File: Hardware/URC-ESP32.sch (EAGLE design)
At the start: 94 parts, among them IC1 MCP9808-MSOP8, IC2 ESPWROOM32, IC3 LM358D, IC4 W5500-LQFP, IC5 CP2102N-A01-GQFN24, J1 SPI-LCD, J10 microSD, J2 I2CBR, J3 USB-C-16P-16P, J4 DC IN, J6 PWR_LED, Q1 FDN340P, Q2 MMDT3904, U1 HY931147C-RJ45

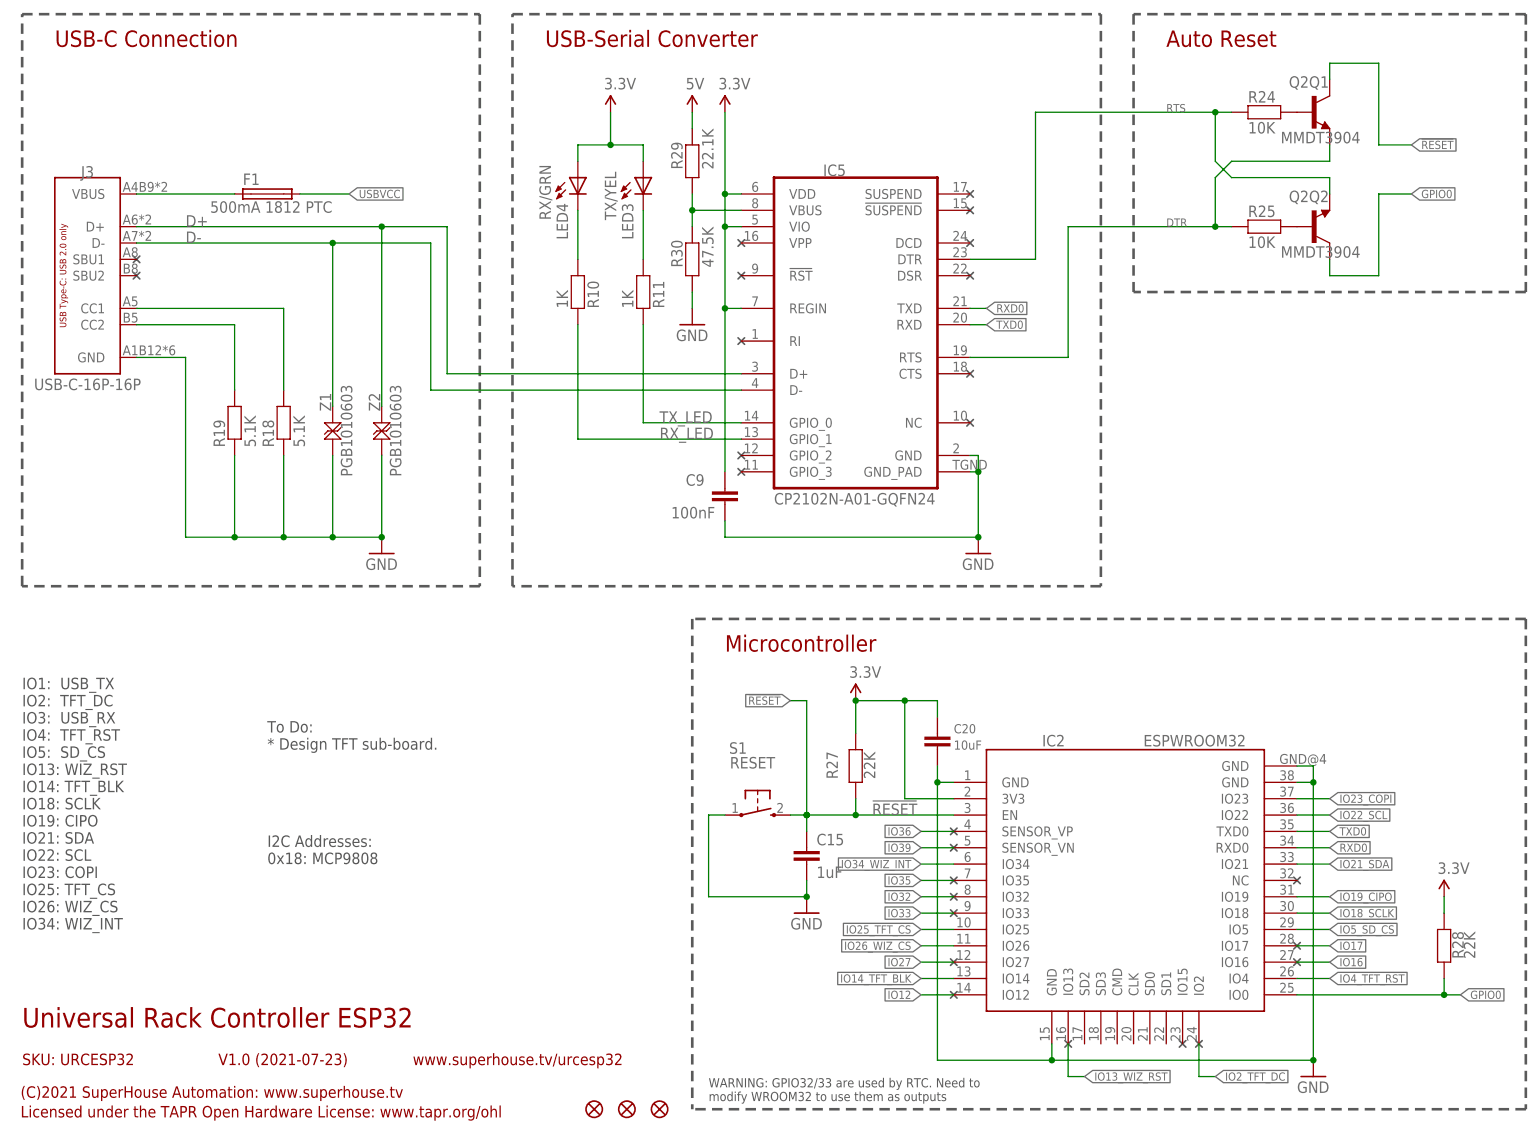
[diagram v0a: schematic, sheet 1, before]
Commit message: Added I/O header with spare pins for I2C port 2 and serial port 2.
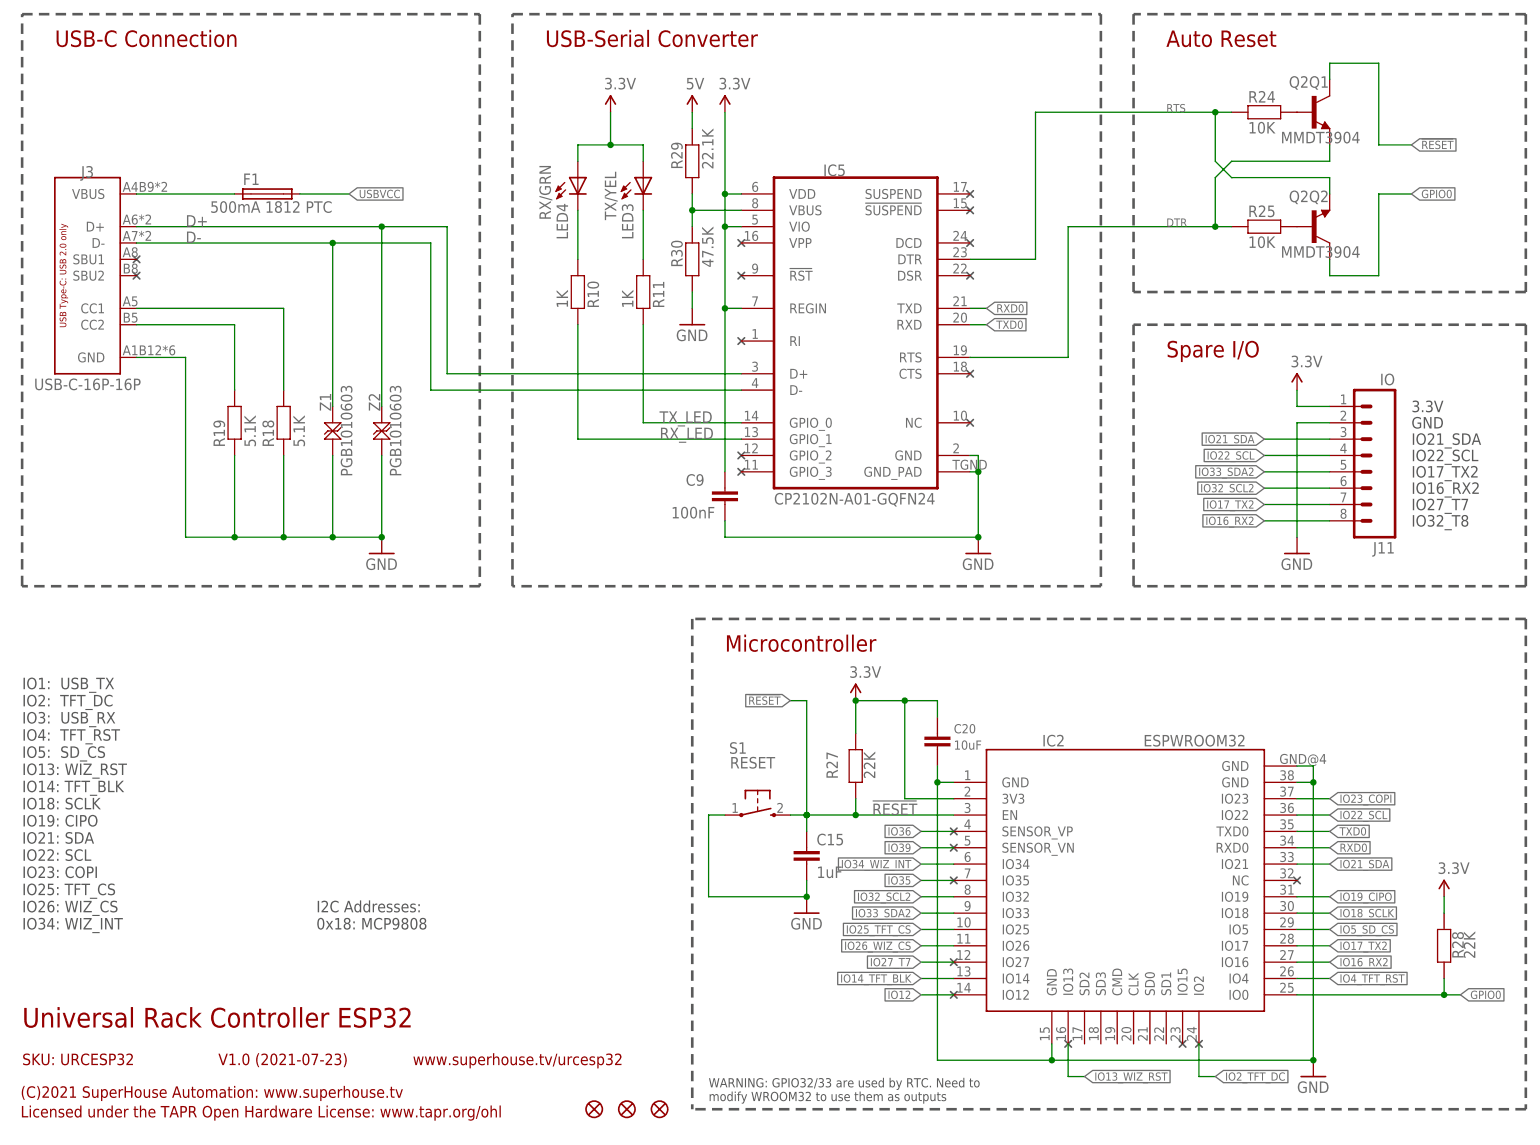
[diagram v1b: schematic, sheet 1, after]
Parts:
- added J11: IO, SuperHouse-Connectors:M08-PLAIN
- C1, C10, C11, C12, C13, C14, C15, C16, C2, C3, C4, C5, C6, C7, C8, C9: device SuperHouse-DiscreteSemi:CAP0603 -> SuperHouse-Capacitors:CAP0603
- C17: device SuperHouse-DiscreteSemi:CAP_POL1206 -> SuperHouse-Capacitors:CAP_POL1206
- C20: device SuperHouse-DiscreteSemi:CAP0805 -> SuperHouse-Capacitors:CAP0805
- D1, D2: device SuperHouse-DiscreteSemi:DIODESMA -> SuperHouse-Diodes:DIODESMA
- Q1: device freetronics-master-v1:MOSFET-PCHANNEL -> SuperHouse-Transistors:MOSFET-PCHANNEL-SMT
- Q2: device SuperHouse-DiscreteSemi:TRANS_NPN_DUAL-MMDT3904 -> SuperHouse-Transistors:TRANS_NPN_DUAL-MMDT3904
- R1, R10, R11, R14, R15, R16, R17, R18, R19, R22, R23, R24, R25, R26, R27, R28, R29, R30, R31: device SuperHouse-DiscreteSemi:RESISTOR0603 -> SuperHouse-Resistors:RESISTOR0603
- RN1, RN2: device SuperHouse-DiscreteSemi:4R-NCAY16 -> SuperHouse-Resistors:4R-NCAY16
- Z1, Z2: device SuperHouse-DiscreteSemi:TVS0603 -> SuperHouse-Diodes:TVS0603
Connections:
- net IO27 renamed IO27_T7
- removed net IO16: IC2.IO16
- removed net IO17: IC2.IO17
- removed net IO32: IC2.IO32
- removed net IO33: IC2.IO33
- new net IO16_RX2: IC2.IO16, J11.8
- new net IO17_TX2: IC2.IO17, J11.7
- new net IO32_SCL2: IC2.IO32, J11.6
- new net IO33_SDA2: IC2.IO33, J11.5
- net 3.3V: now also J11.1
- net GND: now also J11.2
- net IO21_SDA: now also J11.3
- net IO22_SCL: now also J11.4
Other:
- note added: "3.3V"
- note added: "GND"
- note added: "IO16_RX2"
- note added: "IO17_TX2"
- note added: "IO21_SDA"
- note added: "IO22_SCL"
- note added: "IO27_T7"
- note added: "IO32_T8"
- note added: "Spare I/O"
- note removed: "To Do: * Design TFT sub-board."

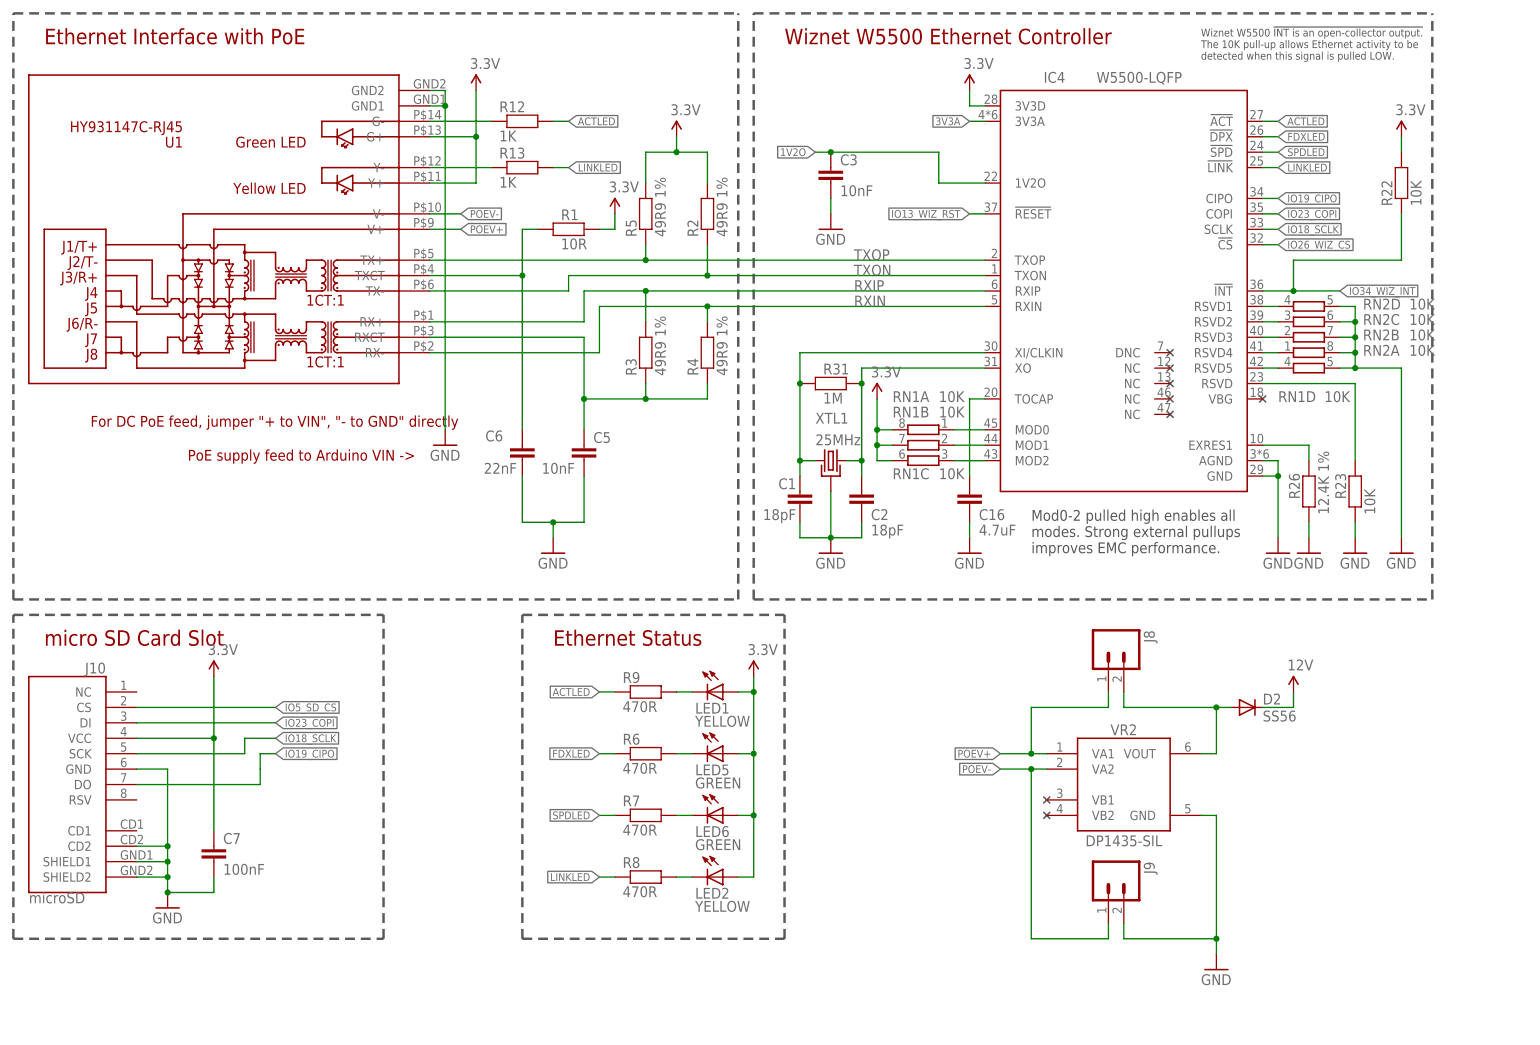
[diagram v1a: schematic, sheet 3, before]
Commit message: Fixed pin allocation notes and labels in schematic. Renamed mechanical PDF to clarify its purpose. Generated schematic PDF.
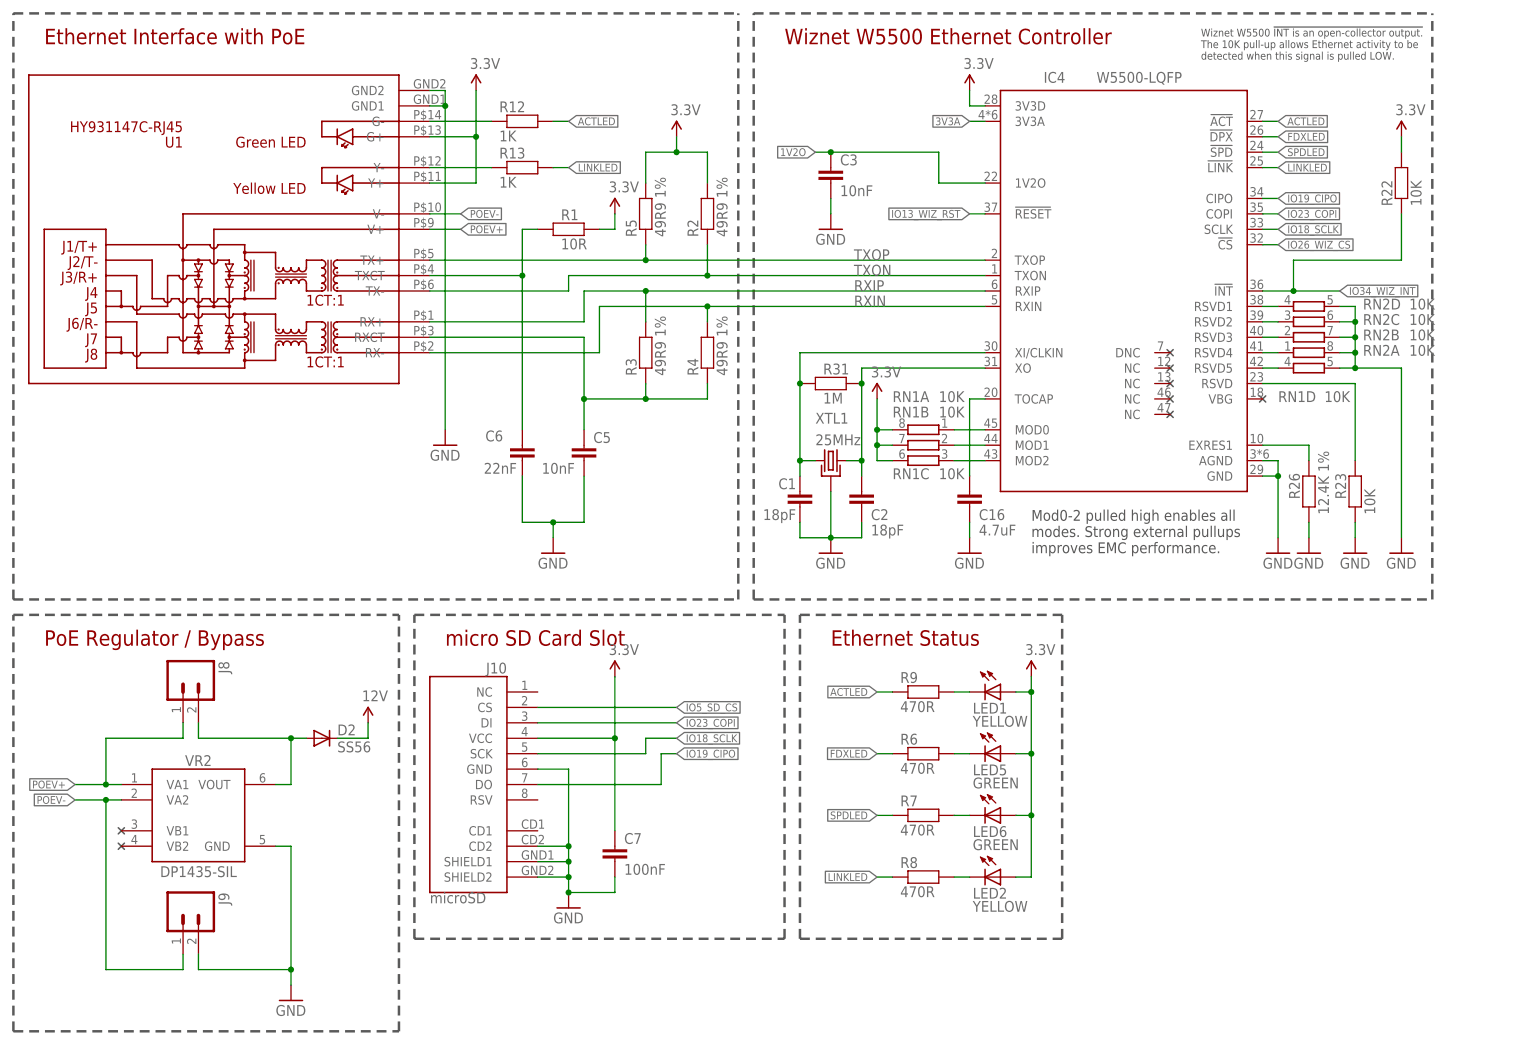
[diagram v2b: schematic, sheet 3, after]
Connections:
- net IO27_T7 renamed IO27
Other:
- note added: "ESP32 Pin Assignment: IO1: USB_TX IO2: TFT_DC IO3: USB_RX IO4: TFT_RST IO5: SD_CS IO13: WIZ_RST IO14: TFT_BLK IO16: RX2 IO17: TX2 IO18: SCLK IO19: CIPO IO21: SDA IO22: SCL IO23: COPI IO25: TFT_CS IO26: WIZ_CS IO32: SCL2 IO33: SDA2 IO34: WIZ_INT"
- note added: "IO32_SCL2"
- note added: "IO33_SDA2"
- note added: "PoE Regulator / Bypass"
- note removed: "For DC PoE feed, jumper "+ to VIN", "- to GND" directly"
- note removed: "IO1: USB_TX IO2: TFT_DC IO3: USB_RX IO4: TFT_RST IO5: SD_CS IO13: WIZ_RST IO14: TFT_BLK IO18: SCLK IO19: CIPO IO21: SDA IO22: SCL IO23: COPI IO25: TFT_CS IO26: WIZ_CS IO34: WIZ_INT"
- note removed: "IO27_T7"
- note removed: "IO32_T8"
- note removed: "PoE supply feed to Arduino VIN ->"
- moved on the sheet: C7, D2, J10, J8, J9, LED1, LED2, LED5, LED6, R6, R7, R8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

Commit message: Minor updates to boards.
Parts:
- LED1: value YELLOW -> GREEN
- R12, R13: value 1K -> 470R
- R27, R28: value 22K -> 10K
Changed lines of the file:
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@@
 <part name="C10" library="SuperHouse-Capacitors" library_urn="urn:adsk.eagle:library:28961179" deviceset="CAP" device="0603" package3d_urn="urn:adsk.eagle:package:7066315/6" value="100nF"/>
 <part name="R31" library="SuperHouse-Resistors" library_urn="urn:adsk.eagle:library:28961094" deviceset="RESISTOR" device="0603" package3d_urn="urn:adsk.eagle:package:28961141/1" value="1M"/>
-<part name="LED1" library="SuperHouse-LEDs" library_urn="urn:adsk.eagle:library:11790571" deviceset="LED" device="0603" package3d_urn="urn:adsk.eagle:package:7066240/3" value="YELLOW"/>
+<part name="LED1" library="SuperHouse-LEDs" library_urn="urn:adsk.eagle:library:11790571" deviceset="LED" device="0603" package3d_urn="urn:adsk.eagle:package:7066240/3" value="GREEN"/>
 <part name="LED5" library="SuperHouse-LEDs" library_urn="urn:adsk.eagle:library:11790571" deviceset="LED" device="0603" package3d_urn="urn:adsk.eagle:package:7066240/3" value="GREEN"/>
 <part name="LED6" library="SuperHouse-LEDs" library_urn="urn:adsk.eagle:library:11790571" deviceset="LED" device="0603" package3d_urn="urn:adsk.eagle:package:7066240/3" value="GREEN"/>
@@
 <part name="J3" library="SuperHouse-Connectors" library_urn="urn:adsk.eagle:library:11765989" deviceset="USB-C-16P" device="-16P" package3d_urn="urn:adsk.eagle:package:17045956/2"/>
 <part name="GND16" library="SuperHouse-SupplySymbols" library_urn="urn:adsk.eagle:library:11790503" deviceset="GND" device=""/>
-<part name="R27" library="SuperHouse-Resistors" library_urn="urn:adsk.eagle:library:28961094" deviceset="RESISTOR" device="0603" package3d_urn="urn:adsk.eagle:package:28961141/1" value="22K"/>
+<part name="R27" library="SuperHouse-Resistors" library_urn="urn:adsk.eagle:library:28961094" deviceset="RESISTOR" device="0603" package3d_urn="urn:adsk.eagle:package:28961141/1" value="10K"/>
 <part name="S1" library="SuperHouse-Switches" library_urn="urn:adsk.eagle:library:11744182" deviceset="TAC_SWITCH_2PIN" device="SMT" package3d_urn="urn:adsk.eagle:package:11818379/4" value="RESET"/>
 <part name="GND17" library="SuperHouse-SupplySymbols" library_urn="urn:adsk.eagle:library:11790503" deviceset="GND" device=""/>
-<part name="R28" library="SuperHouse-Resistors" library_urn="urn:adsk.eagle:library:28961094" deviceset="RESISTOR" device="0603" package3d_urn="urn:adsk.eagle:package:28961141/1" value="22K"/>
+<part name="R28" library="SuperHouse-Resistors" library_urn="urn:adsk.eagle:library:28961094" deviceset="RESISTOR" device="0603" package3d_urn="urn:adsk.eagle:package:28961141/1" value="10K"/>
 <part name="IC2" library="SuperHouse-MCUs" library_urn="urn:adsk.eagle:library:11815114" deviceset="ESPWROOM32" device="" package3d_urn="urn:adsk.eagle:package:11815117/2"/>
 <part name="C20" library="SuperHouse-Capacitors" library_urn="urn:adsk.eagle:library:28961179" deviceset="CAP" device="0805" package3d_urn="urn:adsk.eagle:package:7066318/4" value="10uF"/>
@@
 <part name="R3" library="SuperHouse-Resistors" library_urn="urn:adsk.eagle:library:28961094" deviceset="RESISTOR" device="0603" package3d_urn="urn:adsk.eagle:package:28961141/1" value="49R9 1%"/>
 <part name="R4" library="SuperHouse-Resistors" library_urn="urn:adsk.eagle:library:28961094" deviceset="RESISTOR" device="0603" package3d_urn="urn:adsk.eagle:package:28961141/1" value="49R9 1%"/>
-<part name="R12" library="SuperHouse-Resistors" library_urn="urn:adsk.eagle:library:28961094" deviceset="RESISTOR" device="0603" package3d_urn="urn:adsk.eagle:package:28961141/1" value="1K"/>
-<part name="R13" library="SuperHouse-Resistors" library_urn="urn:adsk.eagle:library:28961094" deviceset="RESISTOR" device="0603" package3d_urn="urn:adsk.eagle:package:28961141/1" value="1K"/>
+<part name="R12" library="SuperHouse-Resistors" library_urn="urn:adsk.eagle:library:28961094" deviceset="RESISTOR" device="0603" package3d_urn="urn:adsk.eagle:package:28961141/1" value="470R"/>
+<part name="R13" library="SuperHouse-Resistors" library_urn="urn:adsk.eagle:library:28961094" deviceset="RESISTOR" device="0603" package3d_urn="urn:adsk.eagle:package:28961141/1" value="470R"/>
 <part name="R9" library="SuperHouse-Resistors" library_urn="urn:adsk.eagle:library:28961094" deviceset="RESISTOR" device="0603" package3d_urn="urn:adsk.eagle:package:28961141/1" value="470R"/>
 <part name="R6" library="SuperHouse-Resistors" library_urn="urn:adsk.eagle:library:28961094" deviceset="RESISTOR" device="0603" package3d_urn="urn:adsk.eagle:package:28961141/1" value="470R"/>
